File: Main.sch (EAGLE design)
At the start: 38 parts

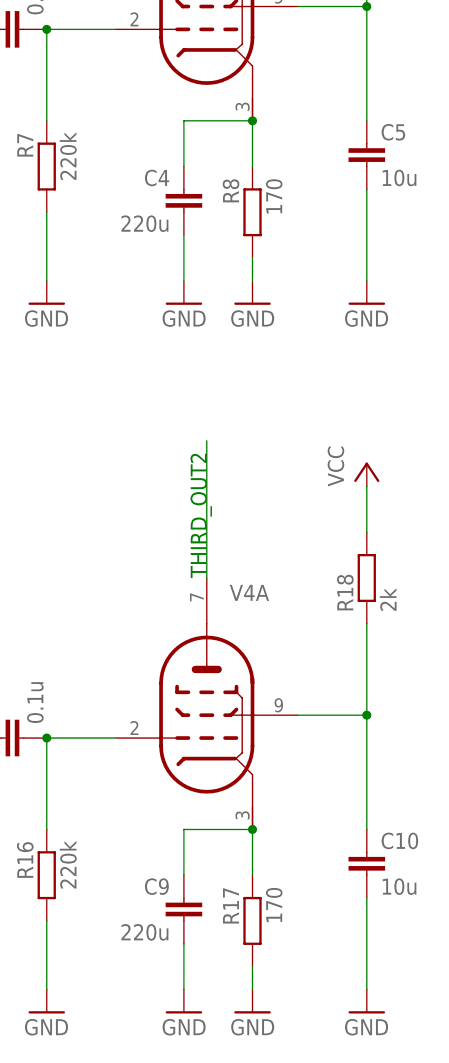
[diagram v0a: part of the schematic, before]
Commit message: [fix]スクリーングリッドの抵抗値と容量を変化
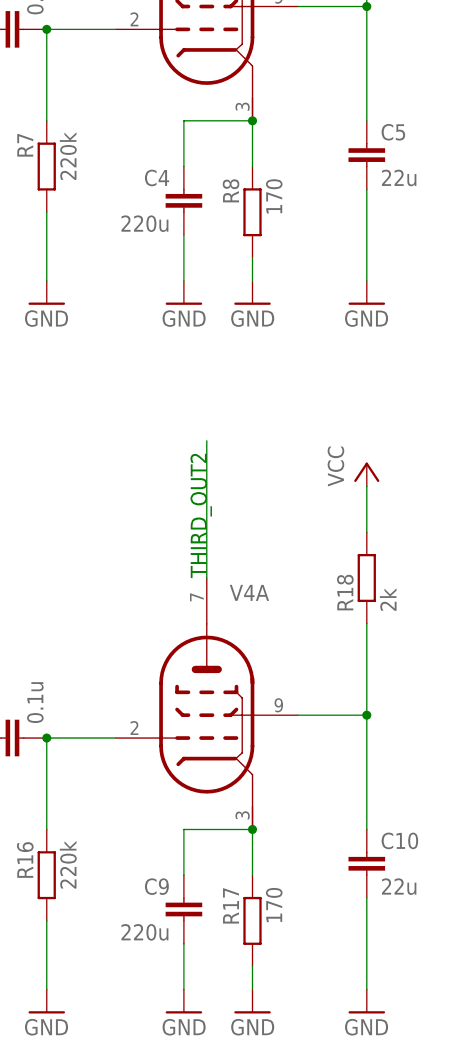
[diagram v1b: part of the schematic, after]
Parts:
- C10, C5: value 10u -> 22u
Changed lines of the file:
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@@
 <part name="R8" library="VacuumTube" library_urn="urn:adsk.eagle:library:8044196" deviceset="RESISTOR2" device="" package3d_urn="urn:adsk.eagle:package:8969348/1" value="170"/>
 <part name="GND12" library="VacuumTube" library_urn="urn:adsk.eagle:library:8044196" deviceset="GND" device=""/>
-<part name="C5" library="VacuumTube" library_urn="urn:adsk.eagle:library:8044196" deviceset="C" device="" package3d_urn="urn:adsk.eagle:package:8969349/1" value="10u"/>
+<part name="C5" library="VacuumTube" library_urn="urn:adsk.eagle:library:8044196" deviceset="C" device="" package3d_urn="urn:adsk.eagle:package:8969349/1" value="22u"/>
 <part name="P+8" library="VacuumTube" library_urn="urn:adsk.eagle:library:8044196" deviceset="VCC" device=""/>
 <part name="GND13" library="VacuumTube" library_urn="urn:adsk.eagle:library:8044196" deviceset="GND" device=""/>
@@
 <part name="R17" library="VacuumTube" library_urn="urn:adsk.eagle:library:8044196" deviceset="RESISTOR2" device="" package3d_urn="urn:adsk.eagle:package:8969348/1" value="170"/>
 <part name="GND21" library="VacuumTube" library_urn="urn:adsk.eagle:library:8044196" deviceset="GND" device=""/>
-<part name="C10" library="VacuumTube" library_urn="urn:adsk.eagle:library:8044196" deviceset="C" device="" package3d_urn="urn:adsk.eagle:package:8969349/1" value="10u"/>
+<part name="C10" library="VacuumTube" library_urn="urn:adsk.eagle:library:8044196" deviceset="C" device="" package3d_urn="urn:adsk.eagle:package:8969349/1" value="22u"/>
 <part name="P+16" library="VacuumTube" library_urn="urn:adsk.eagle:library:8044196" deviceset="VCC" device=""/>
 <part name="GND22" library="VacuumTube" library_urn="urn:adsk.eagle:library:8044196" deviceset="GND" device=""/>

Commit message: [fix]直し
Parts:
- removed C10: 22u, VacuumTube:C
- removed C9: 220u, VacuumTube:C
- removed R18, R9: 2k, VacuumTube:RESISTOR2
- C4: device VacuumTube:C -> VacuumTube:CAPACITOR2
- C5: value 22u -> 220u; device VacuumTube:C -> VacuumTube:CAPACITOR2
- R11, R2: value 3.83k -> 3.9k
- R12, R3: value 50k -> 51k
- R17, R8: value 170 -> 180
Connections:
- removed net N$11: V1C.H3, V3C.H3
- removed net VCC/2: HEATER_VCC.2, V1C.H1, V2B.H1, V3C.H1, V4B.H1
- net GND: now also C4.-, C5.-; no longer C10.2, C4.2, C5.2, C9.2
- net N$14: now also C4.+; no longer C4.1
- net N$17: no longer C5.1, R9.1
- net N$29: now also C5.+; no longer C9.1
- net N$31: no longer C10.1, R18.1
- net VCC: now also HEATER_VCC.2, V1C.H1, V1C.H3, V2B.H1, V3C.H1, V3C.H3, V4B.H1; no longer R18.2, R9.2
